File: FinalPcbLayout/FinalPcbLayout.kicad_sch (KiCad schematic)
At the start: 19 parts, among them J1 Conn_01x04_Pin, J3 Conn_01x11_Pin, J5 Conn_02x05_Odd_Even, J6 Conn_01x02_Pin, J8 Micro_SD_Card, SW1 SW_Push, U1 ESP32-WROOM-32

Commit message: Sim Disabled
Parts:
- C12, C13, C14, C15, FB1, FB2, H1, H2, H3, H4, J1, J3, J5, J6, J8, R8, SW1, U1, U2: Cost (none) -> 0
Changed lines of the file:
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@@
+      (effects (font (size 1.27 1.27)) hide)
+    )
+    (property "Cost" "0" (at 156.21 123.19 0)
+      (effects (font (size 1.27 1.27)) hide)
+    )
+    (property "Sim.Enable" "0" (at 156.21 123.19 0)
       (effects (font (size 1.27 1.27)) hide)
     )
@@
       (effects (font (size 1.27 1.27)) hide)
     )
+    (property "Cost" "0" (at 22.86 58.42 0)
+      (effects (font (size 1.27 1.27)) hide)
+    )
+    (property "Sim.Enable" "0" (at 22.86 58.42 0)
+      (effects (font (size 1.27 1.27)) hide)
+    )
     (instances
       (project "FinalPcbLayout"
@@
     )
     (property "Datasheet" "https://www.espressif.com/sites/default/files/documentation/esp32-wroom-32_datasheet_en.pdf" (at 59.69 60.96 0)
+      (effects (font (size 1.27 1.27)) hide)
+    )
+    (property "Sim.Enable" "0" (at 67.31 62.23 0)
+      (effects (font (size 1.27 1.27)) hide)
+    )
+    (property "Cost" "0" (at 67.31 62.23 0)
       (effects (font (size 1.27 1.27)) hide)
     )
@@
       (effects (font (size 1.27 1.27)) hide)
     )
+    (property "Cost" "0" (at 135.89 133.35 0)
+      (effects (font (size 1.27 1.27)) hide)
+    )
+    (property "Sim.Enable" "0" (at 135.89 133.35 0)
+      (effects (font (size 1.27 1.27)) hide)
+    )
     (pin "1")
     (pin "10")
@@
     )
     (property "Datasheet" "~" (at 232.41 104.14 0)
+      (effects (font (size 1.27 1.27)) hide)
+    )
+    (property "Cost" "0" (at 232.41 104.14 0)
+      (effects (font (size 1.27 1.27)) hide)
+    )
+    (property "Sim.Enable" "0" (at 232.41 104.14 0)
       (effects (font (size 1.27 1.27)) hide)
     )
@@
       (effects (font (size 1.27 1.27)) hide)
     )
+    (property "Cost" "0" (at 152.4 135.89 0)
+      (effects (font (size 1.27 1.27)) hide)
+    )
+    (property "Sim.Enable" "0" (at 152.4 135.89 0)
+      (effects (font (size 1.27 1.27)) hide)
+    )
     (pin "1")
     (pin "2")
@@
       (effects (font (size 1.27 1.27)) hide)
     )
+    (property "Cost" "0" (at 35.56 21.59 0)
+      (effects (font (size 1.27 1.27)) hide)
+    )
+    (property "Sim.Enable" "0" (at 35.56 21.59 0)
+      (effects (font (size 1.27 1.27)) hide)
+    )
     (pin "1")
     (pin "2")
@@
     )
     (property "Datasheet" "http://katalog.we-online.de/em/datasheet/693072010801.pdf" (at 62.23 158.75 0)
+      (effects (font (size 1.27 1.27)) hide)
+    )
+    (property "Cost" "0" (at 62.23 139.7 0)
+      (effects (font (size 1.27 1.27)) hide)
+    )
+    (property "Sim.Enable" "0" (at 62.23 139.7 0)
       (effects (font (size 1.27 1.27)) hide)
     )
@@
       (effects (font (size 1.27 1.27)) hide)
     )
+    (property "Cost" "0" (at 190.5 125.73 0)
+      (effects (font (size 1.27 1.27)) hide)
+    )
+    (property "Sim.Enable" "0" (at 190.5 125.73 0)
+      (effects (font (size 1.27 1.27)) hide)
+    )
     (pin "1")
     (pin "2")
@@
       (effects (font (size 1.27 1.27)) hide)
     )
+    (property "Cost" "0" (at 22.86 67.31 0)
+      (effects (font (size 1.27 1.27)) hide)
+    )
+    (property "Sim.Enable" "0" (at 22.86 67.31 0)
+      (effects (font (size 1.27 1.27)) hide)
+    )
     (instances
       (project "FinalPcbLayout"
@@
     )
     (property "Datasheet" "~" (at 163.83 139.7 0)
+      (effects (font (size 1.27 1.27)) hide)
+    )
+    (property "Cost" "0" (at 163.83 139.7 0)
+      (effects (font (size 1.27 1.27)) hide)
+    )
+    (property "Sim.Enable" "0" (at 163.83 139.7 0)
       (effects (font (size 1.27 1.27)) hide)
     )
@@
       (effects (font (size 1.27 1.27)) hide)
     )
+    (property "Cost" "0" (at 236.22 133.35 0)
+      (effects (font (size 1.27 1.27)) hide)
+    )
+    (property "Sim.Enable" "0" (at 236.22 133.35 0)
+      (effects (font (size 1.27 1.27)) hide)
+    )
     (pin "1")
     (pin "2")
@@
       (effects (font (size 1.27 1.27)) hide)
     )
+    (property "Cost" "0" (at 175.26 139.7 0)
+      (effects (font (size 1.27 1.27)) hide)
+    )
+    (property "Sim.Enable" "0" (at 175.26 139.7 0)
+      (effects (font (size 1.27 1.27)) hide)
+    )
     (pin "1")
     (pin "2")
@@
     )
     (property "Datasheet" "~" (at 22.86 80.01 0)
+      (effects (font (size 1.27 1.27)) hide)
+    )
+    (property "Cost" "0" (at 22.86 80.01 0)
+      (effects (font (size 1.27 1.27)) hide)
+    )
+    (property "Sim.Enable" "0" (at 22.86 80.01 0)
       (effects (font (size 1.27 1.27)) hide)
     )
@@
       (effects (font (size 1.27 1.27)) hide)
     )
+    (property "Cost" "0" (at 102.87 148.59 0)
+      (effects (font (size 1.27 1.27)) hide)
+    )
+    (property "Sim.Enable" "0" (at 102.87 148.59 0)
+      (effects (font (size 1.27 1.27)) hide)
+    )
     (pin "1")
     (pin "2")
@@
     )
     (property "Datasheet" "~" (at 109.22 118.11 0)
+      (effects (font (size 1.27 1.27)) hide)
+    )
+    (property "Cost" "0" (at 109.22 118.11 0)
+      (effects (font (size 1.27 1.27)) hide)
+    )
+    (property "Sim.Enable" "0" (at 109.22 118.11 0)
       (effects (font (size 1.27 1.27)) hide)
     )
@@
       (effects (font (size 1.27 1.27)) (justify right))
     )
-    (property "Value" "Conn_01x11_Pin" (at 128.27 74.93 0)
+    (property "Value" "Conn_01x11_Pin" (at 125.73 68.58 90)
       (effects (font (size 1.27 1.27)) (justify right))
     )
@@
     )
     (property "Datasheet" "~" (at 120.65 77.47 0)
+      (effects (font (size 1.27 1.27)) hide)
+    )
+    (property "Cost" "0" (at 120.65 77.47 0)
+      (effects (font (size 1.27 1.27)) hide)
+    )
+    (property "Sim.Enable" "0" (at 120.65 77.47 0)
       (effects (font (size 1.27 1.27)) hide)
     )
@@
       (effects (font (size 1.27 1.27)) hide)
     )
+    (property "Cost" "0" (at 22.86 88.9 0)
+      (effects (font (size 1.27 1.27)) hide)
+    )
+    (property "Sim.Enable" "0" (at 22.86 88.9 0)
+      (effects (font (size 1.27 1.27)) hide)
+    )
     (instances
       (project "FinalPcbLayout"
@@
       (effects (font (size 1.27 1.27)) hide)
     )
+    (property "Cost" "0" (at 110.49 148.59 0)
+      (effects (font (size 1.27 1.27)) hide)
+    )
+    (property "Sim.Enable" "0" (at 110.49 148.59 0)
+      (effects (font (size 1.27 1.27)) hide)
+    )

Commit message: Update schematic with footprints for power delivery
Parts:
- C12: footprint Capacitor_SMD:C_0603_1608Metric -> Capacitor_SMD:C_0805_2012Metric
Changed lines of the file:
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@@
       (effects (font (size 1.27 1.27)) (justify left))
     )
-    (property "Footprint" "Capacitor_SMD:C_0603_1608Metric" (at 103.8352 152.4 0)
+    (property "Footprint" "Capacitor_SMD:C_0805_2012Metric" (at 103.8352 152.4 0)
       (effects (font (size 1.27 1.27)) hide)
     )

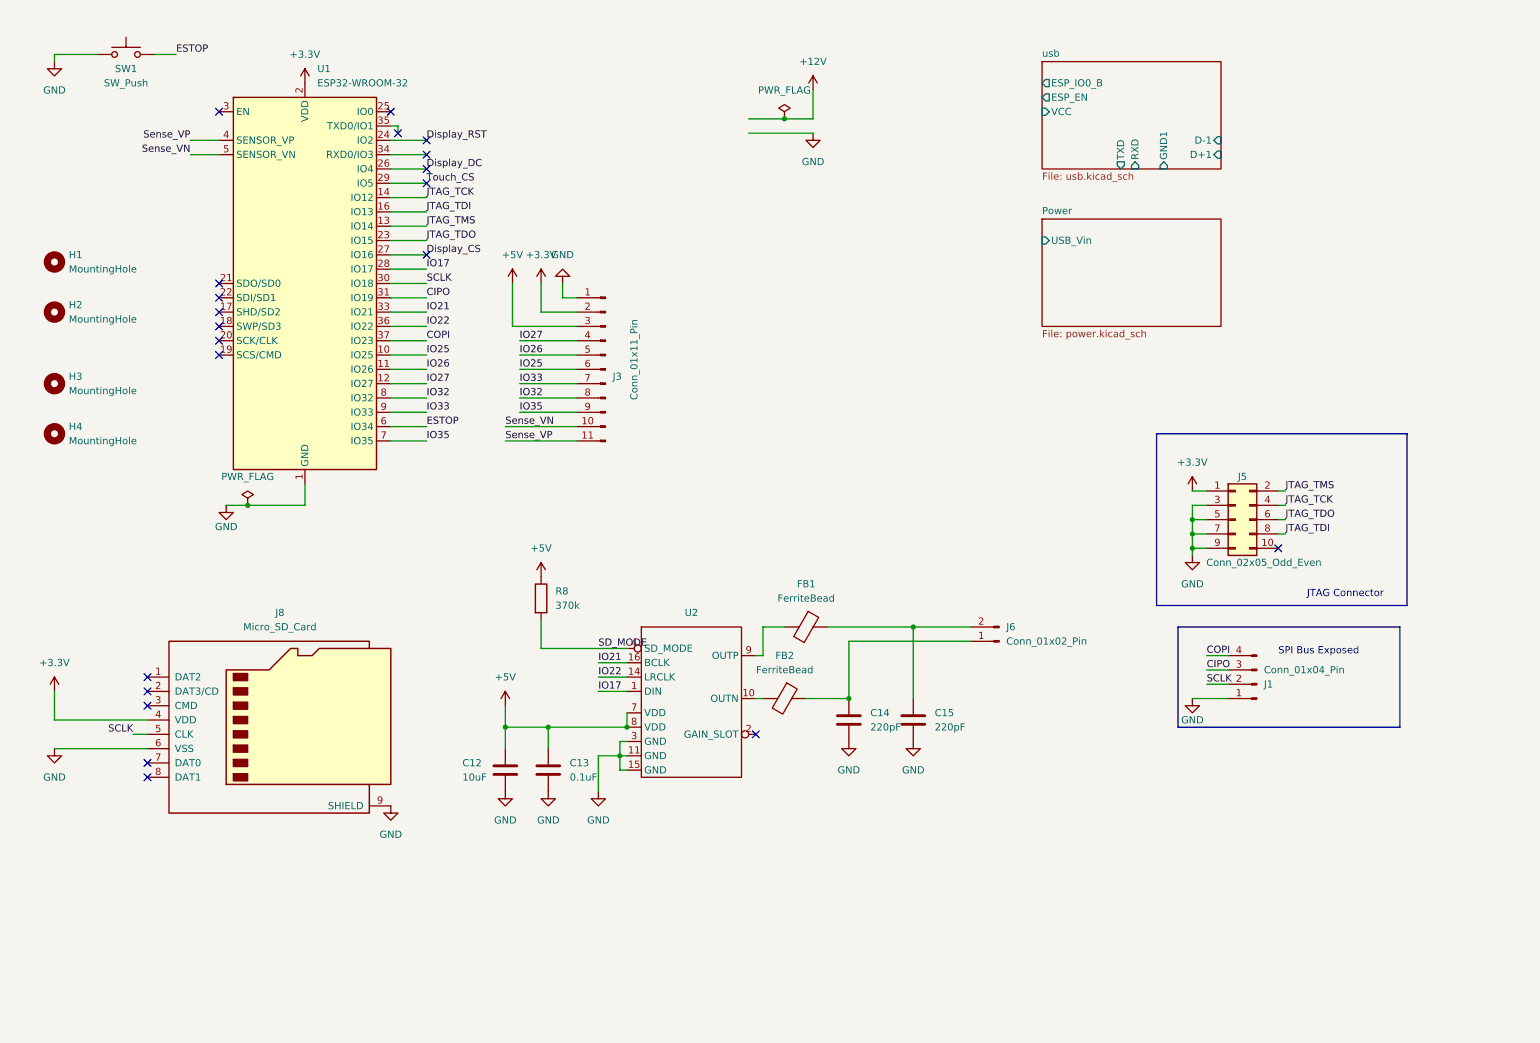
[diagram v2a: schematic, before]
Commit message: No ERC Errors
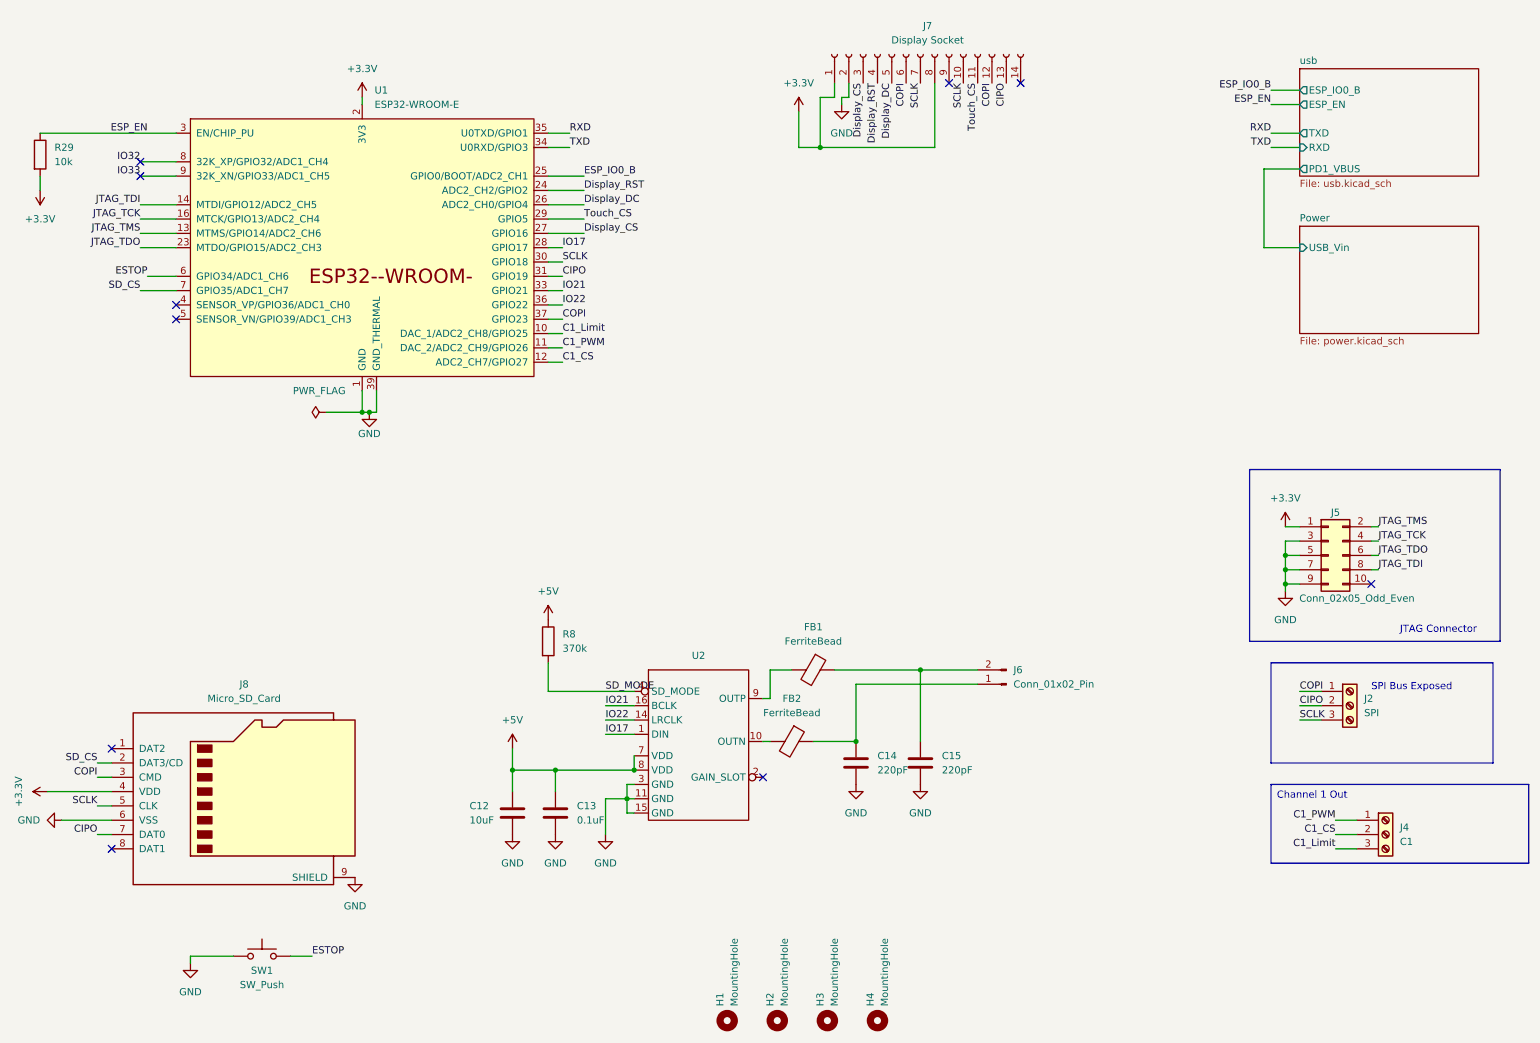
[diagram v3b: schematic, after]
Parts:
- removed J1: Conn_01x04_Pin, TerminalBlock_TE-Connectivity:TerminalBlock_TE_282834-4_1x04_P2.54mm_Horizontal, symbol Connector:Conn_01x04_Pin
- removed J3: Conn_01x11_Pin, Connector_PinHeader_2.54mm:PinHeader_1x11_P2.54mm_Vertical, symbol Connector:Conn_01x11_Pin
- removed U1: ESP32-WROOM-32, RF_Module:ESP32-WROOM-32, symbol RF_Module:ESP32-WROOM-32
- added J2: SPI, TerminalBlock_TE-Connectivity:TerminalBlock_TE_282834-3_1x03_P2.54mm_Horizontal, symbol Connector:Screw_Terminal_01x03
- added J4: C1, TerminalBlock_TE-Connectivity:TerminalBlock_TE_282834-3_1x03_P2.54mm_Horizontal, symbol Connector:Screw_Terminal_01x03
- added J7: Display Socket, Connector_PinSocket_2.54mm:PinSocket_1x14_P2.54mm_Vertical, symbol Connector:Conn_01x14_Socket
- added R29: 10k, Resistor_SMD:R_0603_1608Metric, symbol Device:R
- added U1: ESP32-WROOM-E, PCM_Espressif:ESP32-WROOM-32E, symbol PCM_Espressif:ESP32-WROOM-E
- FB1, FB2: footprint Ferrite_THT:LairdTech_28C0236-0JW-10 -> Resistor_SMD:R_0603_1608Metric; Cost 0 -> .2; digikey_pn (none) -> 445-181518-6-ND
- J5: footprint Connector_PinHeader_2.54mm:PinHeader_2x05_P2.54mm_Vertical -> Connector_PinHeader_1.27mm:PinHeader_2x05_P1.27mm_Vertical
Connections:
- net +3.3V: now also J7.1 (Pin_1), J7.8 (Pin_8), R29.2, U1.2 (3V3)
- net CIPO: now also J8.7 (DAT0), J2.2 (Pin_2), J7.13 (Pin_13), U1.31 (GPIO19)
- net COPI: now also J8.3 (CMD), J2.1 (Pin_1), J7.12 (Pin_12), J7.6 (Pin_6), U1.37 (GPIO23)
- net Display_CS: now also J7.3 (Pin_3), U1.27 (GPIO16)
- net Display_DC: now also J7.5 (Pin_5), U1.26 (ADC2_CH0/GPIO4)
- net Display_RST: now also J7.4 (Pin_4), U1.24 (ADC2_CH2/GPIO2)
- net ESTOP: now also U1.6 (GPIO34/ADC1_CH6)
- net GND: now also J7.2 (Pin_2), U1.1 (GND), U1.15 (GND), U1.38 (GND), U1.39 (GND_THERMAL)
- net IO17: now also U1.28 (GPIO17)
- net IO21: now also U1.33 (GPIO21)
- net IO22: now also U1.36 (GPIO22)
- net IO32: now also U1.8 (32K_XP/GPIO32/ADC1_CH4)
- net IO33: now also U1.9 (32K_XN/GPIO33/ADC1_CH5)
- net JTAG_TCK: now also U1.16 (MTCK/GPIO13/ADC2_CH4)
- net JTAG_TDI: now also U1.14 (MTDI/GPIO12/ADC2_CH5)
- net JTAG_TDO: now also U1.23 (MTDO/GPIO15/ADC2_CH3)
- net JTAG_TMS: now also U1.13 (MTMS/GPIO14/ADC2_CH6)
- net SCLK: now also J2.3 (Pin_3), J7.10 (Pin_10), J7.7 (Pin_7), U1.30 (GPIO18)
- net Touch_CS: now also J7.11 (Pin_11), U1.29 (GPIO5)
- net SD_CS: now reaches J8.2 (DAT3/CD)
- net SD_CS: now also U1.7 (GPIO35/ADC1_CH7)
- new net C1_CS: J4.2 (Pin_2), U1.12 (ADC2_CH7/GPIO27)
- new net C1_Limit: J4.3 (Pin_3), U1.10 (DAC_1/ADC2_CH8/GPIO25)
- new net C1_PWM: J4.1 (Pin_1), U1.11 (DAC_2/ADC2_CH9/GPIO26)
- new net ESP_EN: R29.1, U1.3 (EN/CHIP_PU)
- new net ESP_IO0_B: U1.25 (GPIO0/BOOT/ADC2_CH1)
- new net RXD: U1.35 (U0TXD/GPIO1)
- new net TXD: U1.34 (U0RXD/GPIO3)
- no-connect marks 21 -> 10
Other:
- sheet usb ports: added PD1_VBUS; removed D+1, D-1, GND1, VCC
- moved on the sheet: C12, C13, C14, C15, FB1, H1, H2, H3, H4, J5, J6, J8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
